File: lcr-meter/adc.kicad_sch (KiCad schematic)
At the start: 0 parts

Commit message: Added CM4, basics of functionality started
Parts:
- added U2: MCP3201, symbol Analog_ADC:MCP3201
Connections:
- new net +3V3: U2.8 (Vdd)
- new net +5V: U2.1 (Vref)
- new net GND: U2.4 (Vss)

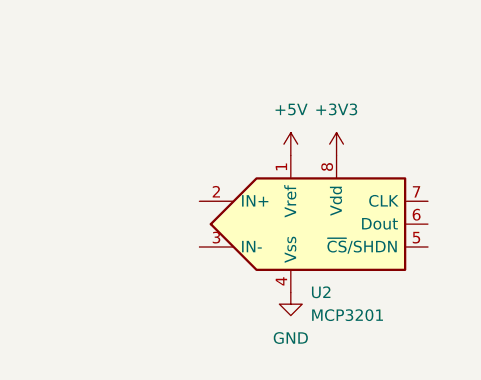
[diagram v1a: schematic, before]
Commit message: Progress, removal of unnecessary components
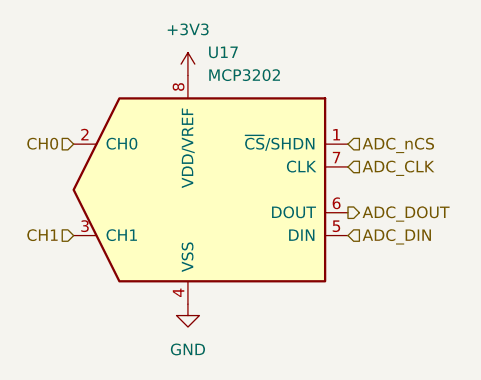
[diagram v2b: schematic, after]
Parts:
- removed U2: MCP3201, symbol Analog_ADC:MCP3201
- added U17: MCP3202, symbol Analog_ADC:MCP3202
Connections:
- net +3V3: now also U17.8 (VDD/VREF)
- net GND: now also U17.4 (VSS)
- new net ADC_CLK: U17.7 (CLK)
- new net ADC_DIN: U17.5 (DIN)
- new net ADC_DOUT: U17.6 (DOUT)
- new net ADC_nCS: U17.1 (~{CS}/SHDN)
- new net CH0: U17.2 (CH0)
- new net CH1: U17.3 (CH1)
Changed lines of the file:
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@@
 	(generator_version "8.0")
 	(paper "A4")
+	(hierarchical_label "CH0"
+		(shape input)
+		(at 125.73 85.09 180)
+		(fields_autoplaced yes)
+		(effects
+			(font
+				(size 1.27 1.27)
+			)
+			(justify right)
+		)
+	)
+	(hierarchical_label "ADC_DIN"
+		(shape input)
+		(at 156.21 95.25 0)
+		(fields_autoplaced yes)
+		(effects
+			(font
+				(size 1.27 1.27)
+			)
+			(justify left)
+		)
+	)
+	(hierarchical_label "CH1"
+		(shape input)
+		(at 125.73 95.25 180)
+		(fields_autoplaced yes)
+		(effects
+			(font
+				(size 1.27 1.27)
+			)
+			(justify right)
+		)
+	)
+	(hierarchical_label "ADC_CLK"
+		(shape input)
+		(at 156.21 87.63 0)
+		(fields_autoplaced yes)
+		(effects
+			(font
+				(size 1.27 1.27)
+			)
+			(justify left)
+		)
+	)
+	(hierarchical_label "ADC_DOUT"
+		(shape output)
+		(at 156.21 92.71 0)
+		(fields_autoplaced yes)
+		(effects
+			(font
+				(size 1.27 1.27)
+			)
+			(justify left)
+		)
+	)
+	(hierarchical_label "ADC_nCS"
+		(shape input)
+		(at 156.21 85.09 0)
+		(fields_autoplaced yes)
+		(effects
+			(font
+				(size 1.27 1.27)
+			)
+			(justify left)
+		)
+	)
 	(symbol
 		(lib_id "power:GND")
-		(at 149.86 101.6 0)
+		(at 138.43 102.87 0)
 		(unit 1)
 		(exclude_from_sim no)
@@
 		(fields_autoplaced yes)
 		(property "Reference" "#PWR039"
-			(at 149.86 107.95 0)
+			(at 138.43 109.22 0)
 			(effects
 				(font
@@
 		)
 		(property "Value" "GND"
-			(at 149.86 106.68 0)
+			(at 138.43 107.95 0)
 			(effects
 				(font
@@
 		)
 		(property "Footprint" ""
-			(at 149.86 101.6 0)
+			(at 138.43 102.87 0)
 			(effects
 				(font
@@
 		)
 		(property "Datasheet" ""
-			(at 149.86 101.6 0)
+			(at 138.43 102.87 0)
 			(effects
 				(font
@@
 		)
 		(property "Description" "Power symbol creates a global label with name \"GND\" , ground"
-			(at 149.86 101.6 0)
+			(at 138.43 102.87 0)
 			(effects
 				(font
@@
 	)
 	(symbol
-		(lib_id "Analog_ADC:MCP3201")
-		(at 152.4 93.98 0)
+		(lib_id "power:+3V3")
+		(at 138.43 77.47 0)
 		(unit 1)
 		(exclude_from_sim no)
@@
 		(dnp no)
 		(fields_autoplaced yes)
-		(property "Reference" "U2"
-			(at 152.0541 101.6 0)
-			(effects
-				(font
-					(size 1.27 1.27)
-				)
-				(justify left)
-			)
-		)
-		(property "Value" "MCP3201"
-			(at 152.0541 104.14 0)
-			(effects
-				(font
-					(size 1.27 1.27)
-				)
-				(justify left)
+		(property "Reference" "#PWR037"
+			(at 138.43 81.28 0)
+			(effects
+				(font
+					(size 1.27 1.27)
+				)
+				(hide yes)
+			)
+		)
+		(property "Value" "+3V3"
+			(at 138.43 72.39 0)
+			(effects
+				(font
+					(size 1.27 1.27)
+				)
 			)
 		)
 		(property "Footprint" ""
-			(at 171.45 102.87 0)
-			(effects
-				(font
-					(size 1.27 1.27)
-				)
-				(hide yes)
-			)
-		)
-		(property "Datasheet" "http://ww1.microchip.com/downloads/en/DeviceDoc/21290D.pdf"
-			(at 172.72 96.52 0)
-			(effects
-				(font
-					(size 1.27 1.27)
-				)
-				(hide yes)
-			)
-		)
-		(property "Description" "2.7V 12-Bit A/D Converter with SPI™ Serial Interface, PDIP-8/SOIC-8/MSOP-8/TSSOP-8"
-			(at 152.4 93.98 0)
-			(effects
-				(font
-					(size 1.27 1.27)
-				)
-				(hide yes)
-			)
-		)
-		(pin "6"
-		)
-		(pin "8"
-		)
-		(pin "2"
-		)
-		(pin "3"
-		)
-		(pin "4"
+			(at 138.43 77.47 0)
+			(effects
+				(font
+					(size 1.27 1.27)
+				)
+				(hide yes)
+			)
+		)
+		(property "Datasheet" ""
+			(at 138.43 77.47 0)
+			(effects
+				(font
+					(size 1.27 1.27)
+				)
+				(hide yes)
+			)
+		)
+		(property "Description" "Power symbol creates a global label with name \"+3V3\""
+			(at 138.43 77.47 0)
+			(effects
+				(font
+					(size 1.27 1.27)
+				)
+				(hide yes)
+			)
 		)
 		(pin "1"
-		)
-		(pin "5"
-		)
-		(pin "7"
 		)
 		(instances
 			(project ""
 				(path "/ba333b18-b098-477b-9dd4-aab7b9764d9c/dc4920c7-bef7-400a-82e9-2e6f0b5b3c21"
-					(reference "U2")
+					(reference "#PWR037")
 					(unit 1)
 				)
@@
 	)
 	(symbol
-		(lib_id "power:+5V")
-		(at 149.86 86.36 0)
+		(lib_id "Analog_ADC:MCP3202")
+		(at 138.43 90.17 0)
 		(unit 1)
 		(exclude_from_sim no)
@@
 		(dnp no)
 		(fields_autoplaced yes)
-		(property "Reference" "#PWR038"
-			(at 149.86 90.17 0)
-			(effects
-				(font
-					(size 1.27 1.27)
-				)
-				(hide yes)
-			)
-		)
-		(property "Value" "+5V"
-			(at 149.86 81.28 0)
-			(effects
-				(font
-					(size 1.27 1.27)
-				)
+		(property "Reference" "U17"
+			(at 140.6241 74.93 0)
+			(effects
+				(font
+					(size 1.27 1.27)
+				)
+				(justify left)
+			)
+		)
+		(property "Value" "MCP3202"
+			(at 140.6241 77.47 0)
+			(effects
+				(font
+					(size 1.27 1.27)
+				)
+				(justify left)
 			)
 		)
 		(property "Footprint" ""
-			(at 149.86 86.36 0)
-			(effects
-				(font
-					(size 1.27 1.27)
-				)
-				(hide yes)
-			)
-		)
-		(property "Datasheet" ""
-			(at 149.86 86.36 0)
-			(effects
-				(font
-					(size 1.27 1.27)
-				)
-				(hide yes)
-			)
-		)
-		(property "Description" "Power symbol creates a global label with name \"+5V\""
-			(at 149.86 86.36 0)
-			(effects
-				(font
-					(size 1.27 1.27)
-				)
-				(hide yes)
-			)
+			(at 138.43 92.71 0)
+			(effects
+				(font
+					(size 1.27 1.27)
+				)
+				(hide yes)
+			)
+		)
+		(property "Datasheet" "http://ww1.microchip.com/downloads/en/DeviceDoc/21034D.pdf"
+			(at 138.43 85.09 0)
+			(effects
+				(font
+					(size 1.27 1.27)
+				)
+				(hide yes)
+			)
+		)
+		(property "Description" "A/D Converter, 12-Bit, 2-Channel, SPI Interface, 2.7V-5.5V"
+			(at 138.43 90.17 0)
+			(effects
+				(font
+					(size 1.27 1.27)
+				)
+				(hide yes)
+			)
+		)
+		(pin "8"
+		)
+		(pin "4"
 		)
 		(pin "1"
+		)
+		(pin "7"
+		)
+		(pin "2"
+		)
+		(pin "5"
+		)
+		(pin "6"
+		)
+		(pin "3"
 		)
 		(instances
 			(project ""
 				(path "/ba333b18-b098-477b-9dd4-aab7b9764d9c/dc4920c7-bef7-400a-82e9-2e6f0b5b3c21"
-					(reference "#PWR038")
+					(reference "U17")
 					(unit 1)
 				)
-			)
-		)
-	)
-	(symbol
-		(lib_id "power:+3V3")
-		(at 154.94 86.36 0)
-		(unit 1)
-		(exclude_from_sim no)
-		(in_bom yes)
-		(on_board yes)
-		(dnp no)
-		(fields_autoplaced yes)
-		(property "Reference" "#PWR037"
-			(at 154.94 90.17 0)
-			(effects
-				(font
-					(size 1.27 1.27)
-				)
-				(hide yes)
-			)
-		)
-		(property "Value" "+3V3"
-			(at 154.94 81.28 0)
-			(effects
-				(font
-					(size 1.27 1.27)
-				)
-			)
-		)
-		(property "Footprint" ""
-			(at 154.94 86.36 0)
-			(effects
-				(font
-					(size 1.27 1.27)
-				)
-				(hide yes)
-			)
-		)
-		(property "Datasheet" ""
-			(at 154.94 86.36 0)
-			(effects
-				(font
-					(size 1.27 1.27)
-				)
-				(hide yes)
-			)
-		)
-		(property "Description" "Power symbol creates a global label with name \"+3V3\""
-			(at 154.94 86.36 0)
-			(effects
-				(font
-					(size 1.27 1.27)
-				)
-				(hide yes)
-			)
-		)
-		(pin "1"
-		)
-		(instances
-			(project ""
-				(path "/ba333b18-b098-477b-9dd4-aab7b9764d9c/dc4920c7-bef7-400a-82e9-2e6f0b5b3c21"
-					(reference "#PWR037")
-					(unit 1)
-				)

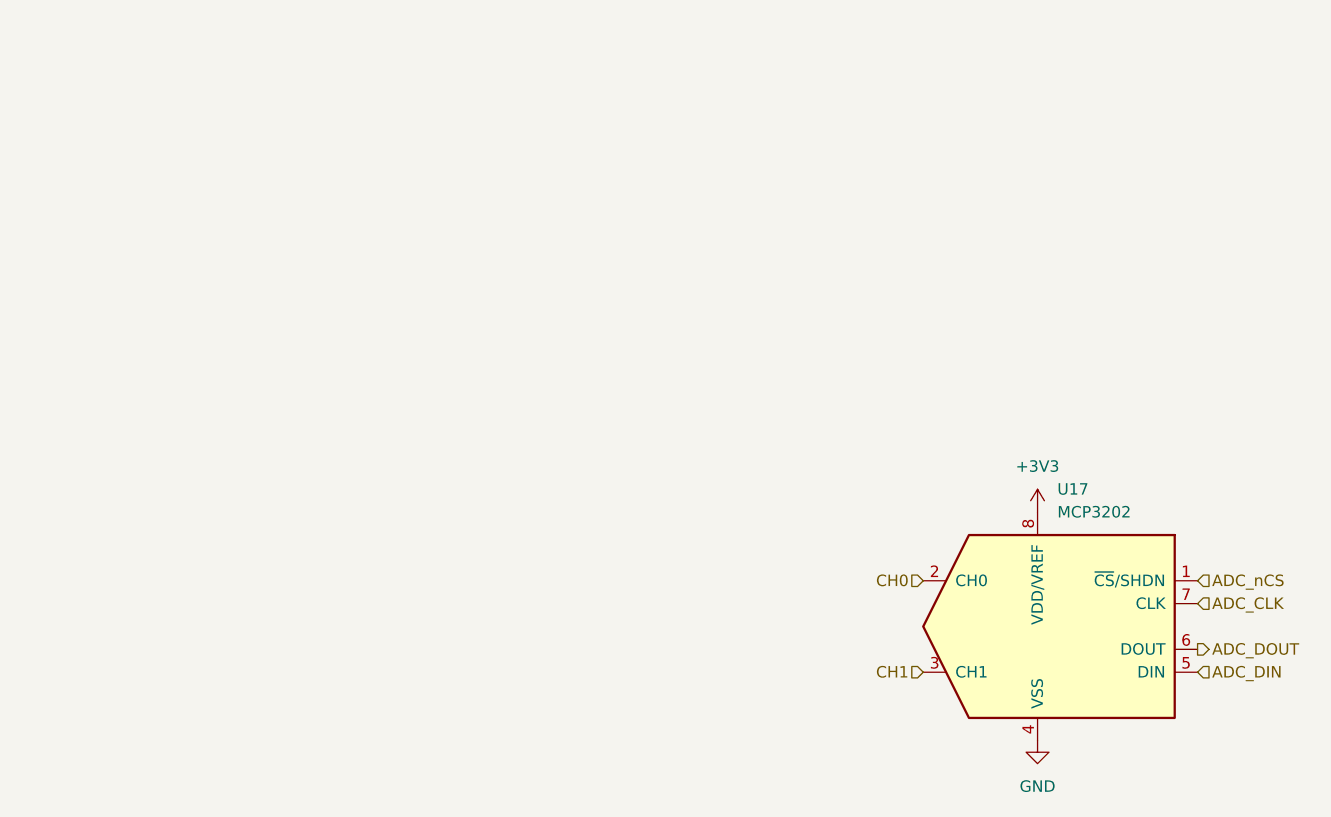
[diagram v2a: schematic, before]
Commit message: Schematic polishing, starting MCU schematic
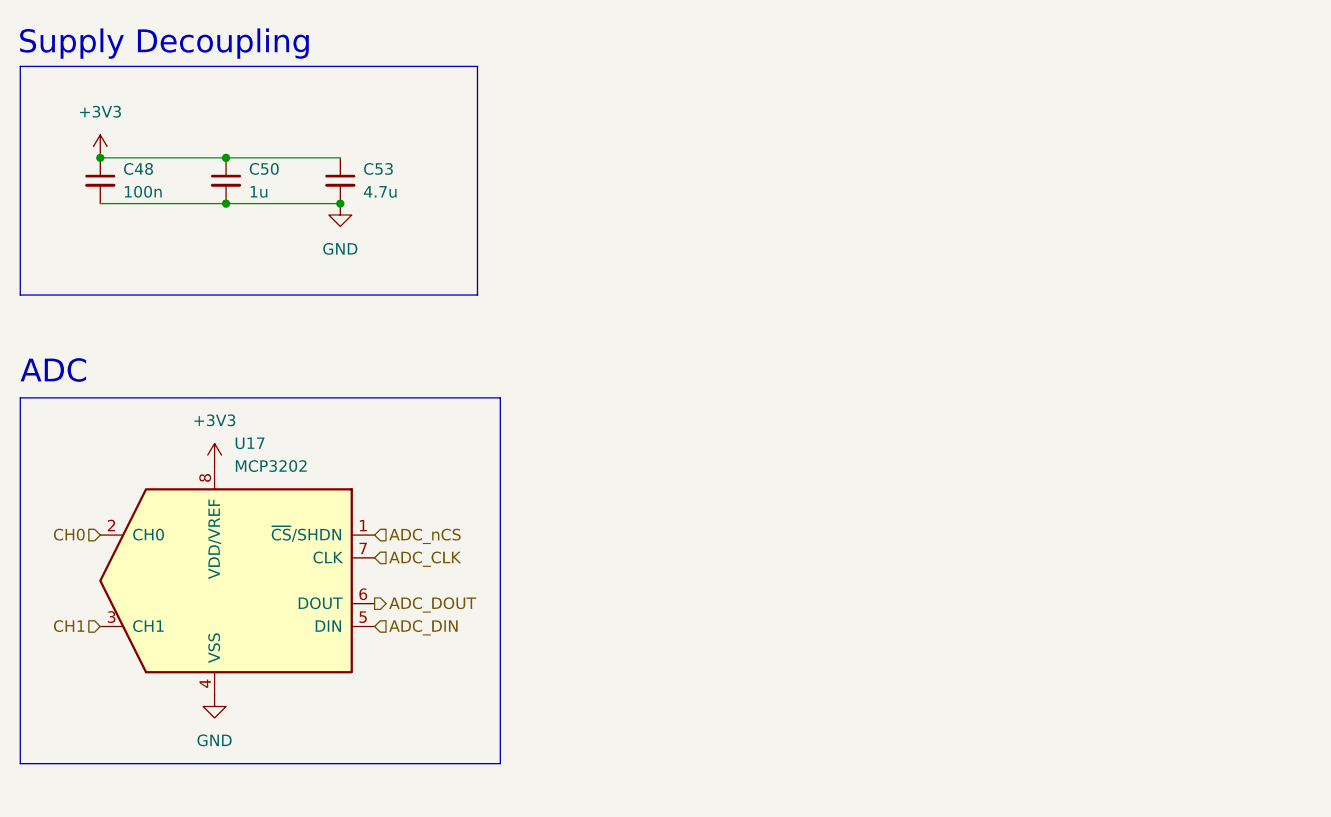
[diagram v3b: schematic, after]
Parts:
- added C48: 100n, Capacitor_SMD:C_0402_1005Metric, symbol Device:C_Small
- added C50: 1u, Capacitor_SMD:C_0402_1005Metric, symbol Device:C_Small
- added C53: 4.7u, Capacitor_SMD:C_0402_1005Metric, symbol Device:C_Small
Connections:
- net +3V3: now also C48.1, C50.1, C53.1
- net GND: now also C48.2, C50.2, C53.2
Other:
- note added: "ADC"
- note added: "Supply Decoupling"
- moved on the sheet: U17

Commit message: Schematic polishing
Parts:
- C53: footprint Capacitor_SMD:C_0402_1005Metric -> Capacitor_SMD:C_0805_2012Metric
- U17: footprint (none) -> Package_DIP:DIP-8_W7.62mm
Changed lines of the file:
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@@
 			)
 		)
-		(property "Footprint" "Capacitor_SMD:C_0402_1005Metric"
+		(property "Footprint" "Capacitor_SMD:C_0805_2012Metric"
 			(at 60.96 40.64 0)
 			(effects
@@
 			)
 		)
-		(property "Footprint" ""
+		(property "Footprint" "Package_DIP:DIP-8_W7.62mm"
 			(at 46.99 87.63 0)
 			(effects
